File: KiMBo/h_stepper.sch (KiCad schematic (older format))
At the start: 24 parts, among them U19 TMC2130

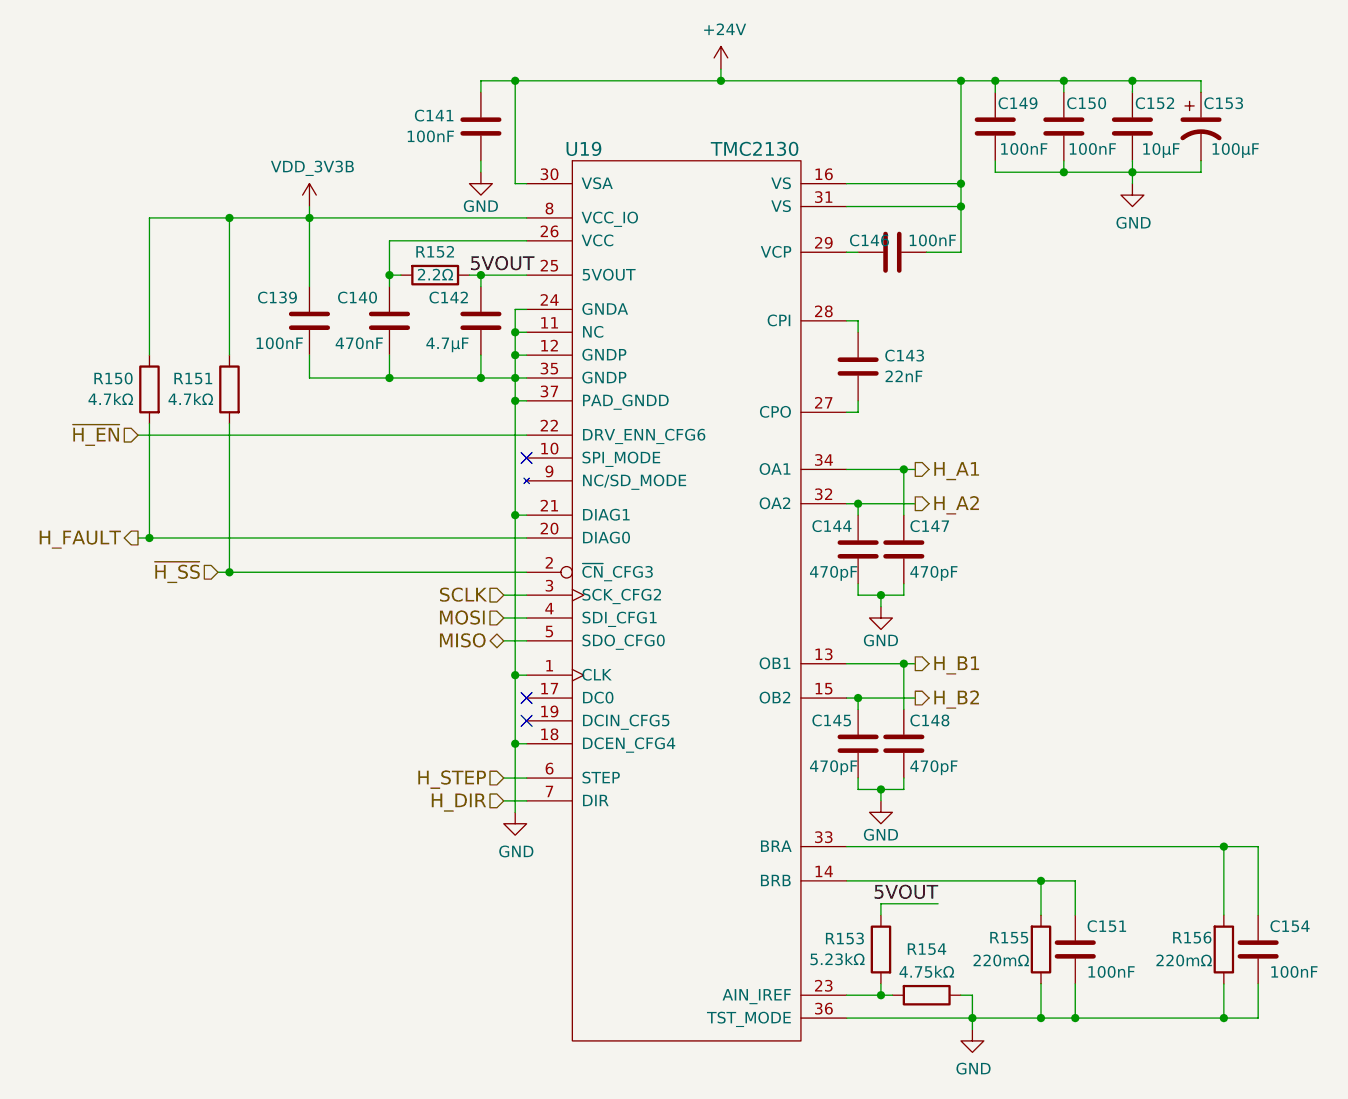
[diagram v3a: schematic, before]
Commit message: Daisy chain the SPI stepper motor driver interface, continue work on the E-heater layout
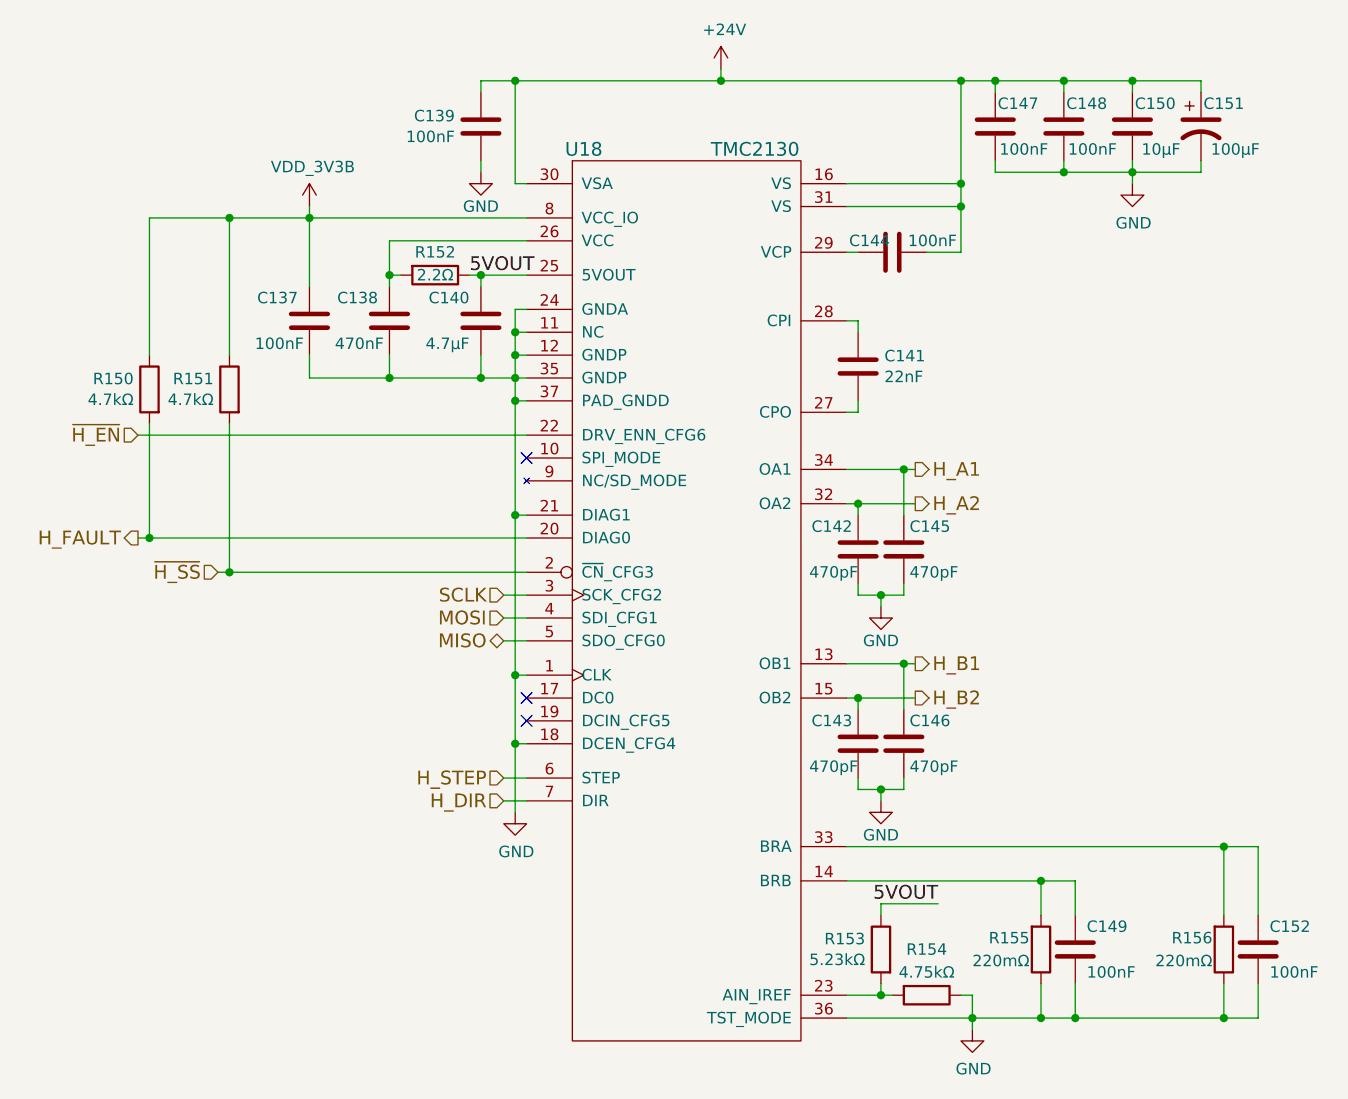
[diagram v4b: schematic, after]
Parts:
- renumbered C139 to C137, C140 to C138, C141 to C139, C142 to C140, C143 to C141, C144 to C142, C145 to C143, C146 to C144, C147 to C145, C148 to C146, C149 to C147, C150 to C148, C151 to C149, C152 to C150, C153 to C151, C154 to C152, U19 to U18
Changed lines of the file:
@@
 MOSI
 $Comp
-L C C141
+L C C139
 U 1 1 5BA7E11E
 P 7300 3950
-F 0 "C141" H 7186 3904 50  0000 R CNN
+F 0 "C139" H 7186 3904 50  0000 R CNN
 F 1 "100nF" H 7186 3995 50  0000 R CNN
 F 2 "Capacitors_SMD:C_0603" H 7338 3800 50  0001 C CNN
@@
 $EndComp
 $Comp
-L C C146
+L C C144
 U 1 1 589B8C70
 P 9100 4500
-F 0 "C146" V 9050 4400 50  0000 C CNN
+F 0 "C144" V 9050 4400 50  0000 C CNN
 F 1 "100nF" V 9050 4675 50  0000 C CNN
 F 2 "Capacitors_SMD:C_0603" H 9138 4350 50  0001 C CNN
@@
 $EndComp
 $Comp
-L CP1 C153
+L CP1 C151
 U 1 1 589B8CBD
 P 10450 3950
-F 0 "C153" H 10550 4050 50  0000 C CNN
+F 0 "C151" H 10550 4050 50  0000 C CNN
 F 1 "100μF" H 10600 3850 50  0000 C CNN
 F 2 "Capacitors_SMD:c_elec_8x10" H 10450 3950 50  0001 C CNN
@@
 $EndComp
 $Comp
-L C C149
+L C C147
 U 1 1 5BA7E121
 P 9550 3950
-F 0 "C149" H 9450 4050 50  0000 C CNN
+F 0 "C147" H 9450 4050 50  0000 C CNN
 F 1 "100nF" H 9425 3850 50  0000 C CNN
 F 2 "Capacitors_SMD:C_0603" H 9588 3800 50  0001 C CNN
@@
 $EndComp
 $Comp
-L GND #PWR0209
+L GND #PWR189
 U 1 1 5BA7E122
 P 7300 4150
-F 0 "#PWR0209" H 7300 3900 50  0001 C CNN
+F 0 "#PWR189" H 7300 3900 50  0001 C CNN
 F 1 "GND" H 7300 4000 50  0000 C CNN
 F 2 "" H 7300 4150 50  0000 C CNN
@@
 $EndComp
 $Comp
-L C C150
+L C C148
 U 1 1 5BA7E123
 P 9850 3950
-F 0 "C150" H 9750 4050 50  0000 C CNN
+F 0 "C148" H 9750 4050 50  0000 C CNN
 F 1 "100nF" H 9725 3850 50  0000 C CNN
 F 2 "Capacitors_SMD:C_0603" H 9888 3800 50  0001 C CNN
@@
 $EndComp
 $Comp
-L GND #PWR0210
+L GND #PWR195
 U 1 1 5BA7E124
 P 10150 4200
-F 0 "#PWR0210" H 10150 3950 50  0001 C CNN
+F 0 "#PWR195" H 10150 3950 50  0001 C CNN
 F 1 "GND" H 10155 4027 50  0000 C CNN
 F 2 "" H 10150 4200 50  0000 C CNN
@@
 $EndComp
 $Comp
-L +24V #PWR0211
+L +24V #PWR191
 U 1 1 589BEDE1
 P 8350 3700
-F 0 "#PWR0211" H 8350 3550 50  0001 C CNN
+F 0 "#PWR191" H 8350 3550 50  0001 C CNN
 F 1 "+24V" H 8365 3873 50  0000 C CNN
 F 2 "" H 8350 3700 50  0000 C CNN
@@
 $EndComp
 $Comp
-L C C143
+L C C141
 U 1 1 5BA7E126
 P 8950 5000
-F 0 "C143" H 9065 5046 50  0000 L CNN
+F 0 "C141" H 9065 5046 50  0000 L CNN
 F 1 "22nF" H 9065 4955 50  0000 L CNN
 F 2 "Capacitors_SMD:C_0603" H 8988 4850 50  0001 C CNN
@@
 $EndComp
 $Comp
-L GND #PWR0212
+L GND #PWR194
 U 1 1 589C2B70
 P 9450 7900
-F 0 "#PWR0212" H 9450 7650 50  0001 C CNN
+F 0 "#PWR194" H 9450 7650 50  0001 C CNN
 F 1 "GND" H 9455 7727 50  0000 C CNN
 F 2 "" H 9450 7900 50  0000 C CNN
@@
 $EndComp
 $Comp
-L C C140
+L C C138
 U 1 1 5BA7E12C
 P 6900 4800
-F 0 "C140" H 6950 4900 50  0000 L CNN
+F 0 "C138" H 6950 4900 50  0000 L CNN
 F 1 "470nF" H 6925 4700 50  0000 L CNN
 F 2 "Capacitors_SMD:C_0603" H 6938 4650 50  0001 C CNN
@@
 NoConn ~ 7500 6550
 $Comp
-L GND #PWR0213
+L GND #PWR190
 U 1 1 5BA7E12D
 P 7450 6950
-F 0 "#PWR0213" H 7450 6700 50  0001 C CNN
+F 0 "#PWR190" H 7450 6700 50  0001 C CNN
 F 1 "GND" H 7455 6777 50  0000 C CNN
 F 2 "" H 7450 6950 50  0000 C CNN
@@
 $EndComp
 $Comp
-L C C151
+L C C149
 U 1 1 589CC9B9
 P 9900 7550
-F 0 "C151" H 9950 7650 50  0000 L CNN
+F 0 "C149" H 9950 7650 50  0000 L CNN
 F 1 "100nF" H 9950 7450 50  0000 L CNN
 F 2 "Capacitors_SMD:C_0603" H 9938 7400 50  0001 C CNN
@@
 NoConn ~ 7500 5400
 $Comp
-L C C142
+L C C140
 U 1 1 589C396E
 P 7300 4800
-F 0 "C142" H 7350 4900 50  0000 L CNN
+F 0 "C140" H 7350 4900 50  0000 L CNN
 F 1 "4.7μF" H 7350 4700 50  0000 L CNN
 F 2 "Capacitors_SMD:C_0603" H 7338 4650 50  0001 C CNN
@@
 $EndComp
 $Comp
-L C C154
+L C C152
 U 1 1 58AF169E
 P 10700 7550
-F 0 "C154" H 10750 7650 50  0000 L CNN
+F 0 "C152" H 10750 7650 50  0000 L CNN
 F 1 "100nF" H 10750 7450 50  0000 L CNN
 F 2 "Capacitors_SMD:C_0603" H 10738 7400 50  0001 C CNN
@@
 $EndComp
 $Comp
-L C C144
+L C C142
 U 1 1 58B19CCF
 P 8950 5800
-F 0 "C144" H 8975 5900 50  0000 L CNN
+F 0 "C142" H 8975 5900 50  0000 L CNN
 F 1 "470pF" H 8950 5700 50  0000 L CNN
 F 2 "Capacitors_SMD:C_0603" H 8988 5650 50  0001 C CNN
@@
 $EndComp
 $Comp
-L GND #PWR0214
+L GND #PWR192
 U 1 1 5BA7E135
 P 9050 6050
-F 0 "#PWR0214" H 9050 5800 50  0001 C CNN
+F 0 "#PWR192" H 9050 5800 50  0001 C CNN
 F 1 "GND" H 9050 5900 50  0000 C CNN
 F 2 "" H 9050 6050 50  0000 C CNN
@@
 $EndComp
 $Comp
-L C C147
+L C C145
 U 1 1 5BA7E136
 P 9150 5800
-F 0 "C147" H 9175 5900 50  0000 L CNN
+F 0 "C145" H 9175 5900 50  0000 L CNN
 F 1 "470pF" H 9175 5700 50  0000 L CNN
 F 2 "Capacitors_SMD:C_0603" H 9188 5650 50  0001 C CNN
@@
 $EndComp
 $Comp
-L C C145
+L C C143
 U 1 1 5BA7E137
 P 8950 6650
-F 0 "C145" H 8975 6750 50  0000 L CNN
+F 0 "C143" H 8975 6750 50  0000 L CNN
 F 1 "470pF" H 8950 6550 50  0000 L CNN
 F 2 "Capacitors_SMD:C_0603" H 8988 6500 50  0001 C CNN
@@
 $EndComp
 $Comp
-L GND #PWR0215
+L GND #PWR193
 U 1 1 5BA7E138
 P 9050 6900
-F 0 "#PWR0215" H 9050 6650 50  0001 C CNN
+F 0 "#PWR193" H 9050 6650 50  0001 C CNN
 F 1 "GND" H 9050 6750 50  0000 C CNN
 F 2 "" H 9050 6900 50  0000 C CNN
@@
 $EndComp
 $Comp
-L C C148
+L C C146
 U 1 1 5BA7E139
 P 9150 6650
-F 0 "C148" H 9175 6750 50  0000 L CNN
+F 0 "C146" H 9175 6750 50  0000 L CNN
 F 1 "470pF" H 9175 6550 50  0000 L CNN
 F 2 "Capacitors_SMD:C_0603" H 9188 6500 50  0001 C CNN
@@
 $EndComp
 $Comp
-L TMC2130 U19
+L TMC2130 U18
 U 1 1 589A7425
 P 8200 5550
-F 0 "U19" H 7750 7050 60  0000 C CNN
+F 0 "U18" H 7750 7050 60  0000 C CNN
 F 1 "TMC2130" H 8500 7050 60  0000 C CNN
 F 2 "KiMBo:QFN36_5X6" H 8200 5850 60  0001 C CNN
@@
 	8950 6850 8950 6800
 $Comp
-L C C152
+L C C150
 U 1 1 5BA7E13A
 P 10150 3950
-F 0 "C152" H 10050 4050 50  0000 C CNN
+F 0 "C150" H 10050 4050 50  0000 C CNN
 F 1 "10μF" H 10025 3850 50  0000 C CNN
 F 2 "Capacitors_SMD:C_0805" H 10188 3800 50  0001 C CNN
@@
 	5850 4350 7500 4350
 $Comp
-L VDD_3V3B #PWR0216
+L VDD_3V3B #PWR188
 U 1 1 5A2FEA7A
 P 6550 4300
-F 0 "#PWR0216" H 6550 4150 50  0001 C CNN
+F 0 "#PWR188" H 6550 4150 50  0001 C CNN
 F 1 "VDD_3V3B" H 6565 4473 50  0000 C CNN
 F 2 "" H 6550 4300 50  0000 C CNN
@@
 $EndComp
 $Comp
-L C C139
+L C C137
 U 1 1 5A897FB1
 P 6550 4800
-F 0 "C139" H 6600 4900 50  0000 L CNN
+F 0 "C137" H 6600 4900 50  0000 L CNN
 F 1 "100nF" H 6575 4700 50  0000 L CNN
 F 2 "Capacitors_SMD:C_0603" H 6588 4650 50  0001 C CNN
